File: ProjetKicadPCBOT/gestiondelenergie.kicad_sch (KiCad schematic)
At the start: 29 parts, among them J6 USB_C_Receptacle_USB2.0_16P, J7 Conn_01x02, SW3 SW_Push, U4 BQ25896, U5 AP2112K-3.3

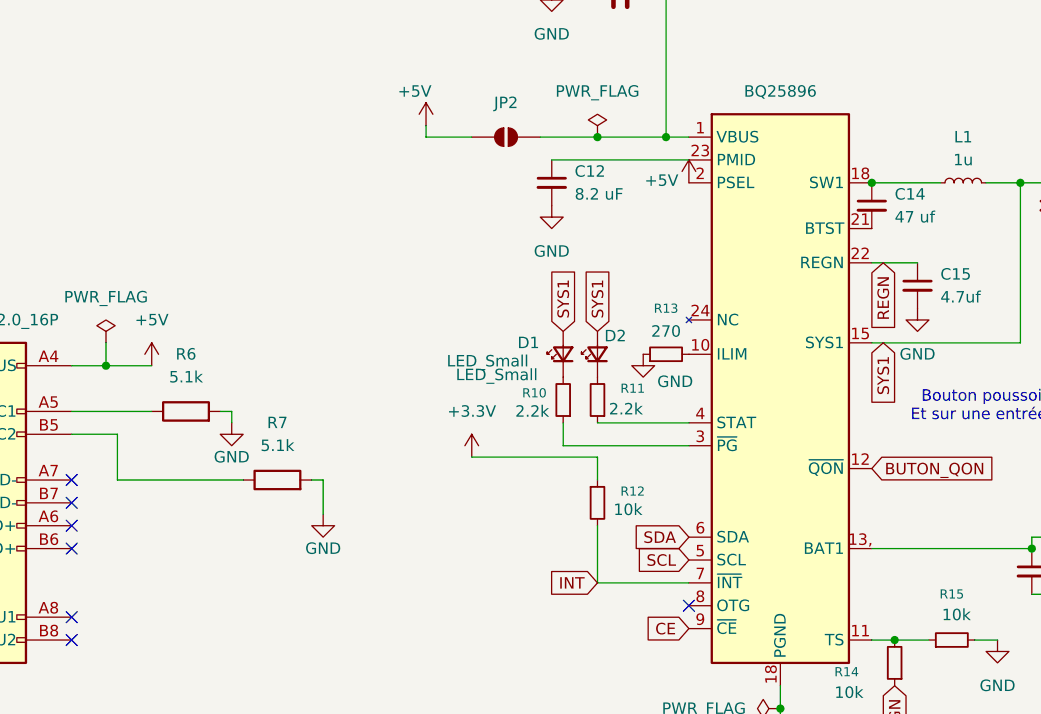
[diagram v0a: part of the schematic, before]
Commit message: Il reste 6 warning et il faut arranger les écritures
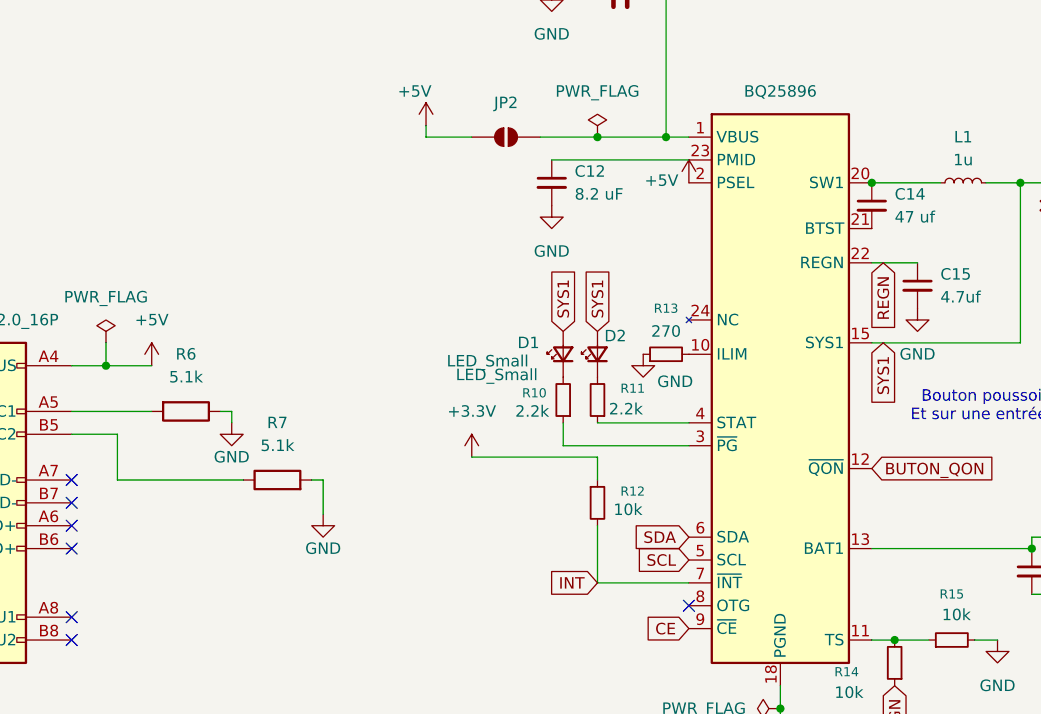
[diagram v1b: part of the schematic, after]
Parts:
- U4: footprint Package_DFN_QFN:Texas_RQM0029A_VQFN-29_4x4mm_P0.4mm -> Package_DFN_QFN:WQFN-24-1EP_4x4mm_P0.5mm_EP2.45x2.45mm_ThermalVias
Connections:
- net GND: now also R6.1, U4.25 (PGND); no longer R6.2
- net at J6.A5 (CC1): now also R6.2; no longer R6.1
- net at C16.1, J7.1 (Pin_1), U4.14 (BAT2): now also U4.13 (BAT1); no longer U4.13, (BAT1)
- net at C14.1, L1.1, U4.19 (SW2): now also U4.20 (SW1); no longer U4.18 (SW1)
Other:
- moved on the sheet: R6
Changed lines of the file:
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@@
+	)
+	(junction
+		(at 204.47 74.93)
+		(diameter 0)
+		(color 0 0 0 0)
+	)
+	(junction
+		(at 120.65 72.39)
+		(diameter 0)
+		(color 0 0 0 0)
 	)
 	(junction
@@
 	)
 	(junction
-		(at 204.47 74.93)
-		(diameter 0)
-		(color 0 0 0 0)
-	)
-	(junction
-		(at 120.65 72.39)
-		(diameter 0)
-		(color 0 0 0 0)
-	)
-	(junction
 		(at 167.64 77.47)
 		(diameter 0)
@@
 	(wire
 		(pts
+			(xy 116.84 104.14) (xy 116.84 106.68)
+		)
+		(stroke
+			(width 0)
+			(type default)
+		)
+	)
+	(wire
+		(pts
 			(xy 115.57 74.93) (xy 130.81 74.93)
 		)
@@
 	(wire
 		(pts
+			(xy 168.91 116.84) (xy 168.91 118.11)
+		)
+		(stroke
+			(width 0)
+			(type default)
+		)
+	)
+	(wire
+		(pts
 			(xy 189.23 119.38) (xy 179.07 119.38)
 		)
@@
 	(wire
 		(pts
+			(xy 116.84 106.68) (xy 130.81 106.68)
+		)
+		(stroke
+			(width 0)
+			(type default)
+		)
+	)
+	(wire
+		(pts
 			(xy 140.97 138.43) (xy 140.97 135.89)
 		)
@@
 	(wire
 		(pts
-			(xy 116.84 106.68) (xy 130.81 106.68)
-		)
-		(stroke
-			(width 0)
-			(type default)
-		)
-	)
-	(wire
-		(pts
 			(xy 91.44 153.67) (xy 91.44 152.4)
 		)
@@
 	(wire
 		(pts
-			(xy 168.91 116.84) (xy 168.91 118.11)
-		)
-		(stroke
-			(width 0)
-			(type default)
-		)
-	)
-	(wire
-		(pts
 			(xy 114.3 72.39) (xy 120.65 72.39)
 		)
@@
 	(wire
 		(pts
+			(xy 151.13 118.11) (xy 168.91 118.11)
+		)
+		(stroke
+			(width 0)
+			(type default)
+		)
+	)
+	(wire
+		(pts
 			(xy 171.45 82.55) (xy 176.53 82.55)
 		)
@@
 	(wire
 		(pts
-			(xy 116.84 104.14) (xy 116.84 106.68)
-		)
-		(stroke
-			(width 0)
-			(type default)
-		)
-	)
-	(wire
-		(pts
 			(xy 106.68 107.95) (xy 120.65 107.95)
 		)
@@
 		(pts
 			(xy 187.96 74.93) (xy 194.31 74.93)
-		)
-		(stroke
-			(width 0)
-			(type default)
-		)
-	)
-	(wire
-		(pts
-			(xy 151.13 118.11) (xy 168.91 118.11)
 		)
 		(stroke
@@
 			)
 		)
-		(property "Footprint" "Package_DFN_QFN:Texas_RQM0029A_VQFN-29_4x4mm_P0.4mm"
+		(property "Footprint" "Package_DFN_QFN:WQFN-24-1EP_4x4mm_P0.5mm_EP2.45x2.45mm_ThermalVias"
 			(at 140.97 162.814 0)
 			(effects
@@
 		(pin "17"
 		)
-		(pin "18"
+		(pin "20"
 		)
 		(pin "19"
@@
 		(pin "16"
 		)
-		(pin "13,"
+		(pin "13"
 		)
 		(pin "15"
@@
 		)
 		(pin "11"
+		)
+		(pin "25"
 		)
 		(instances
@@
 	(symbol
 		(lib_id "PCBot_Lib:R")
-		(at 74.93 102.87 90)
+		(at 74.93 102.87 270)
 		(unit 1)
 		(exclude_from_sim no)
@@
 		)
 		(property "Footprint" "Resistor_SMD:R_0805_2012Metric_Pad1.20x1.40mm_HandSolder"
-			(at 74.93 104.648 90)
-			(effects
-				(font
+			(at 74.93 101.092 90)
+			(effects
+				(font

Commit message: .
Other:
- company: (none) -> ENSEA
- title: PC BOT - Gestion de l'énergie -> PCB BOT rahim 974
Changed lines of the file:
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@@
 	(paper "A4")
 	(title_block
-		(title "PC BOT - Gestion de l'énergie")
-		(date "2026-02-08")
+		(title "PCB BOT rahim 974")
+		(date "2026-02-07")
+		(rev "1.0")
+		(company "ENSEA")
 	)
 	(text "Connecteur USB"
